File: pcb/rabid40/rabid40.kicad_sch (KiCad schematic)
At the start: 115 parts, among them J1 MX-NoLED, K1 MX-NoLED, M1 MX-NoLED, P1 MX-NoLED, Q1 MX-NoLED, SW1 SW_PUSH, T1 MX-NoLED, U1 ATmega32U4-A, U2 MX-NoLED, X1 MX-NoLED, Y1 16MHz, Y2 MX-NoLED

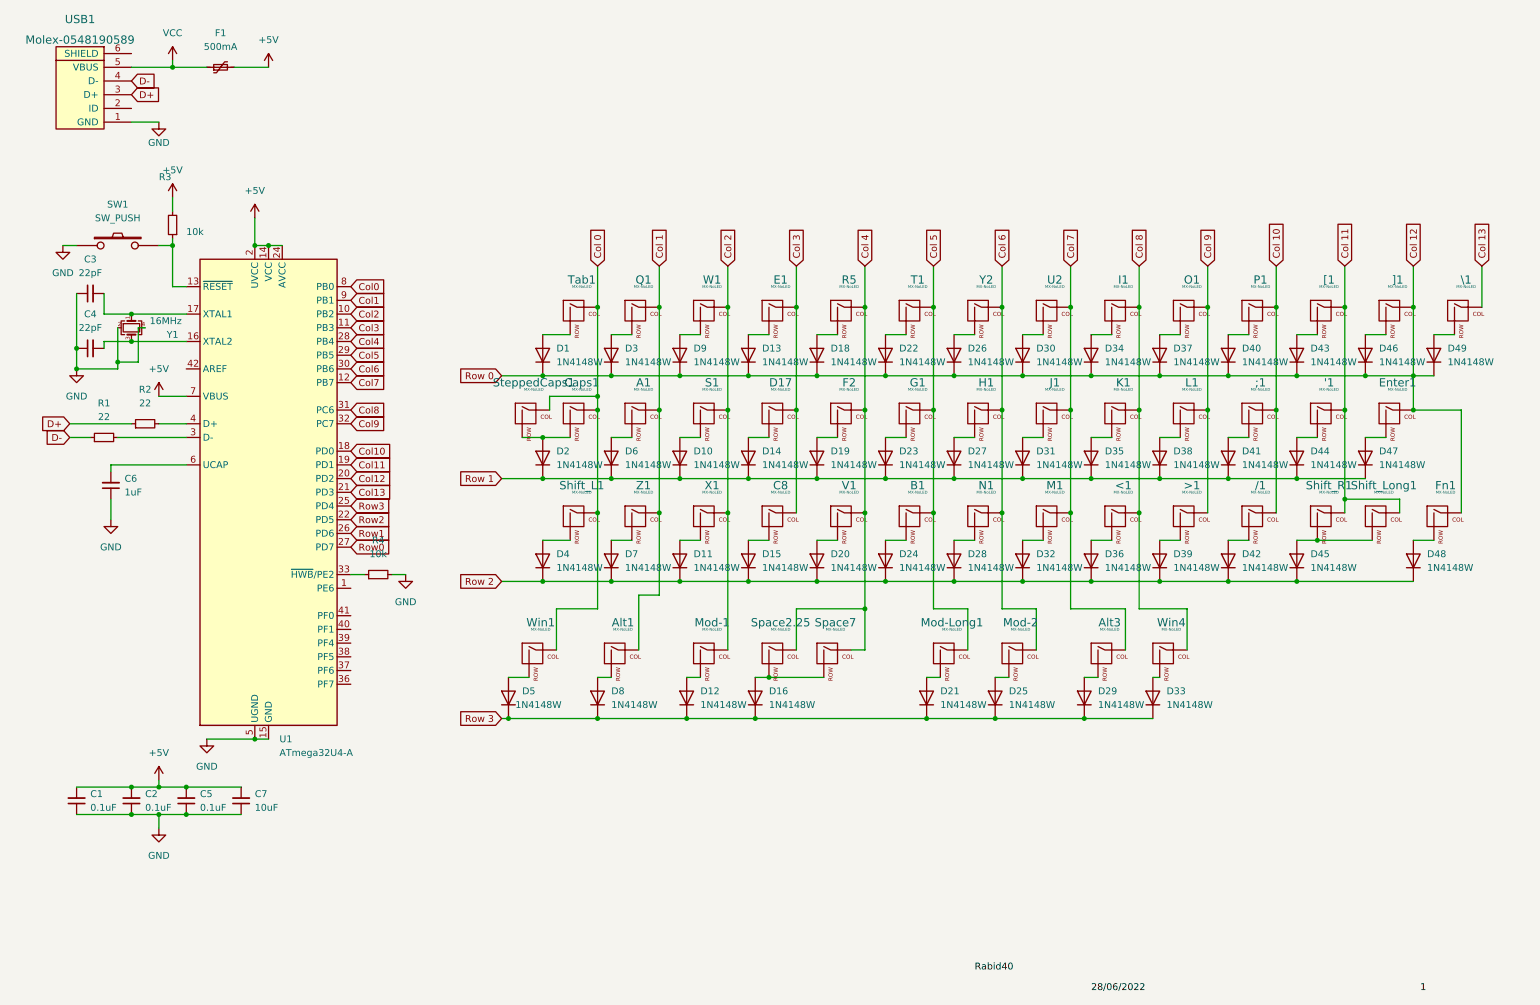
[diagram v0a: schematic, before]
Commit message: reset schematic, added submodules
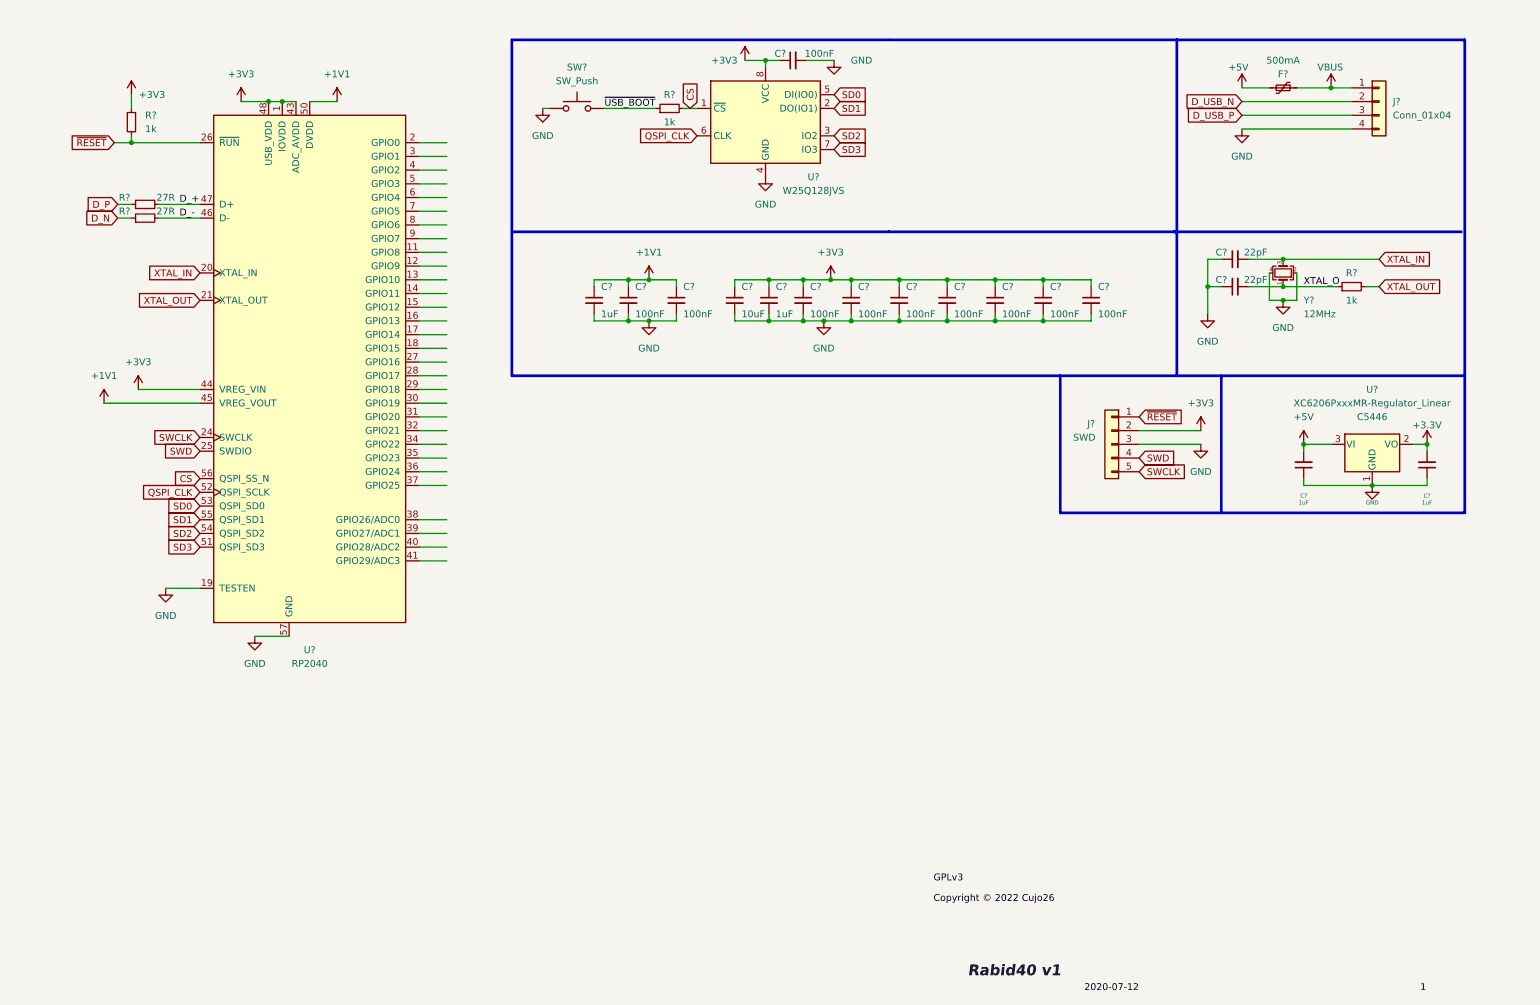
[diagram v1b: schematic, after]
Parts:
- removed '1, /1, ;1, <1, >1, A1, B1, C8, D17, E1, F2, Fn1, G1, H1, I1, J1, K1, L1, M1, Mod-1, Mod-2, N1, O1, P1, Q1, R5, S1, SteppedCaps1, T1, U2, V1, W1, Win1, Win4, X1, Y2, Z1, [1, ]1: MX-NoLED, MX_Alps_Hybrid:MX-1U, symbol ai03-mx-alps-hybrid:MX-NoLED
- removed Alt1, Alt3, Tab1, \1: MX-NoLED, MX_Alps_Hybrid:MX-1.5U, symbol ai03-mx-alps-hybrid:MX-NoLED
- removed C1, C2, C5: 0.1uF, Capacitor_SMD:C_0805_2012Metric, symbol Device:C_Small
- removed C3, C4: 22pF, Capacitor_SMD:C_0805_2012Metric, symbol Device:C_Small
- removed C6: 1uF, Capacitor_SMD:C_0805_2012Metric, symbol Device:C_Small
- removed C7: 10uF, Capacitor_SMD:C_0805_2012Metric, symbol Device:C_Small
- removed Caps1, Shift_R1: MX-NoLED, MX_Alps_Hybrid:MX-1.75U, symbol ai03-mx-alps-hybrid:MX-NoLED
- removed D1, D10, D11, D12, D13, D14, D15, D16, D18, D19, D2, D20, D21, D22, D23, D24, D25, D26, D27, D28, D29, D3, D30, D31, D32, D33, D34, D35, D36, D37, D38, D39, D4, D40, D41, D42, D43, D44, D45, D46, D47, D48, D49, D5, D6, D7, D8, D9: 1N4148W, Diode_SMD:D_SOD-123, symbol Diode:1N4148W
- removed Enter1, Shift_L1, Space2.25: MX-NoLED, MX_Alps_Hybrid:MX-2.25U, symbol ai03-mx-alps-hybrid:MX-NoLED
- removed F1: 500mA, Fuse:Fuse_1206_3216Metric, symbol Device:Polyfuse_Small
- removed Mod-Long1, Shift_Long1: MX-NoLED, MX_Alps_Hybrid:MX-2.75U, symbol ai03-mx-alps-hybrid:MX-NoLED
- removed R1, R2: 22, Resistor_SMD:R_0805_2012Metric, symbol Device:R_Small
- removed R3, R4: 10k, Resistor_SMD:R_0805_2012Metric, symbol Device:R_Small
- removed SW1: SW_PUSH, random-keyboard-parts:SKQG-1155865, symbol Keyboard_Symbols:SW_PUSH
- removed Space7: MX-NoLED, MX_Alps_Hybrid:MX-7U, symbol ai03-mx-alps-hybrid:MX-NoLED
- removed U1: ATmega32U4-A, Package_QFP:TQFP-44_10x10mm_P0.8mm, symbol MCU_Microchip_ATmega:ATmega32U4-A
- removed USB1: Molex-0548190589, random-keyboard-parts:Molex-0548190589, symbol ai03-random-parts:Molex-0548190589
- removed Y1: 16MHz, Crystal:Crystal_SMD_3225-4Pin_3.2x2.5mm, symbol Device:Crystal_GND24_Small
- added C? (x2): 22pF, Capacitor_SMD:C_0402_1005Metric, symbol Device:C_Small
- added C? (x4): 1uF, Capacitor_SMD:C_0402_1005Metric, symbol Device:C_Small
- added C? (x10): 100nF, Capacitor_SMD:C_0402_1005Metric, symbol Device:C_Small
- added C?: 10uF, Capacitor_SMD:C_0402_1005Metric, symbol Device:C_Small
- added F?: 500mA, Fuse:Fuse_1206_3216Metric, symbol Device:Polyfuse_Small
- added J?: SWD, Connector_PinSocket_2.54mm:PinSocket_1x05_P2.54mm_Vertical, symbol Connector_Generic:Conn_01x05
- added J?: Conn_01x04, symbol Connector_Generic:Conn_01x04
- added R? (x2): 27R, Resistor_SMD:R_0603_1608Metric, symbol Device:R_Small
- added R? (x3): 1k, Resistor_SMD:R_0402_1005Metric, symbol Device:R_Small
- added SW?: SW_Push, Connector_PinSocket_2.54mm:PinSocket_1x02_P2.54mm_Vertical, symbol Switch:SW_Push
- added U?: W25Q128JVS, Package_SO:SOIC-8_5.23x5.23mm_P1.27mm, symbol Memory_Flash:W25Q128JVS
- added U?: RP2040, Sleep-Lib:RP2040-QFN-56, symbol Sleep-lib:RP2040
- added U?: XC6206PxxxMR-Regulator_Linear, Package_TO_SOT_SMD:SOT-23, symbol kicad-keyboard-parts:XC6206PxxxMR-Regulator_Linear
- added Y?: 12MHz, Crystal:Crystal_SMD_3225-4Pin_3.2x2.5mm, symbol Device:Crystal_GND24_Small
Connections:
- net +5V: now also C?.2, F?.2, U?.3 (VI)
- net GND: now also C?.1, C?.1, C?.1, C?.1, C?.2, C?.2, C?.2, C?.2, C?.2, C?.2, C?.2, C?.2, C?.2, C?.2, C?.2, C?.2, C?.2, J?.3 (Pin_3), J?.4 (Pin_4), SW?.1, U?.1 (GND), U?.19 (TESTEN), U?.4 (GND), U?.57 (GND), Y?.2, Y?.4
- new net +1V1: C?.1, C?.1, C?.1, U?.23 (DVDD), U?.45 (VREG_VOUT), U?.50 (DVDD)
- new net +3V3: C?.1, C?.1, C?.1, C?.1, C?.1, C?.1, C?.1, C?.1, C?.1, C?.1, C?.2, J?.2 (Pin_2), R?.1, U?.1 (IOVDD), U?.10 (IOVDD), U?.2 (VO), U?.22 (IOVDD), U?.33 (IOVDD), U?.42 (IOVDD), U?.43 (ADC_AVDD), U?.44 (VREG_VIN), U?.48 (USB_VDD), U?.49 (IOVDD), U?.8 (VCC)
- new net CS: R?.2, U?.1 (~{CS}), U?.56 (QSPI_SS_N)
- new net D_+: R?.2, U?.47 (D+)
- new net D_-: R?.2, U?.46 (D-)
- new net D_N: R?.1
- new net D_P: R?.1
- new net D_USB_N: J?.2 (Pin_2)
- new net D_USB_P: J?.3 (Pin_3)
- new net QSPI_CLK: U?.52 (QSPI_SCLK), U?.6 (CLK)
- new net SD0: U?.5 (DI(IO0)), U?.53 (QSPI_SD0)
- new net SD1: U?.2 (DO(IO1)), U?.55 (QSPI_SD1)
- new net SD2: U?.3 (IO2), U?.54 (QSPI_SD2)
- new net SD3: U?.51 (QSPI_SD3), U?.7 (IO3)
- new net SWCLK: J?.5 (Pin_5), U?.24 (SWCLK)
- new net SWD: J?.4 (Pin_4), U?.25 (SWDIO)
- new net VBUS: F?.1, J?.1 (Pin_1)
- new net XTAL_IN: C?.2, U?.20 (XTAL_IN), Y?.3
- new net XTAL_O: C?.2, R?.1, Y?.1
- new net XTAL_OUT: R?.2, U?.21 (XTAL_OUT)
- new net ~{RESET}: J?.1 (Pin_1), R?.2, U?.26 (~{RUN})
- new net ~{USB_BOOT}: R?.1, SW?.2

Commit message: files organised
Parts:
- removed C? (x2): 1uF, Capacitor_SMD:C_0402_1005Metric, symbol Device:C_Small
- removed J?: SWD, Connector_PinSocket_2.54mm:PinSocket_1x05_P2.54mm_Vertical, symbol Connector_Generic:Conn_01x05
- removed U?: XC6206PxxxMR-Regulator_Linear, Package_TO_SOT_SMD:SOT-23, symbol kicad-keyboard-parts:XC6206PxxxMR-Regulator_Linear
- added '1, /1, ;1, <1, >1, A1, Alt1, Alt2, B1, C18, D46, E1, Enter1, F2, Fn1, G1, H1, I1, J3, K1, L1, LMod1, M1, N1, O1, P1, Q1, R6, RMod1, S1, Shift1, Shift2, Shift3, Space2.25, Space2.75, Space_7u1, T1, U4, V1, W1, Win1, Win2, X1, Y2, Z1, [1, ]1: MX_SW_solder, marbastlib-mx:SW_MX_1u, symbol marbastlib-mx:MX_SW_solder
- added Bspc1, Tab1: MX_SW_solder, marbastlib-mx:SW_MX_1.5u, symbol marbastlib-mx:MX_SW_solder
- added C11, C15: 1uF, Capacitor_SMD:C_0402_1005Metric, symbol Device:C_Small
- added Ctrl1: MX_SW_solder, marbastlib-mx:SW_MX_1.75u, symbol marbastlib-mx:MX_SW_solder
- added D1, D10, D11, D12, D13, D14, D15, D16, D17, D18, D19, D2, D20, D21, D22, D23, D24, D25, D26, D27, D28, D29, D3, D30, D31, D32, D33, D34, D35, D36, D37, D38, D39, D4, D40, D41, D42, D43, D44, D47, D48, D49, D5, D50, D52, D6, D7, D8, D9: 1N4148W, Diode_SMD:D_SOD-123, symbol Diode:1N4148W
- added J1: SWD, Connector_PinSocket_2.54mm:PinSocket_1x05_P2.54mm_Vertical, symbol Connector_Generic:Conn_01x05
- added Stab_Enter1, Stab_LShift1: MX_stab, marbastlib-mx:STAB_MX_2.25u, symbol marbastlib-mx:MX_stab
- added Stab_RShift1: MX_stab, marbastlib-mx:STAB_MX_2.75u, symbol marbastlib-mx:MX_stab
- added Stab_Spc2.25: MX_stab, marbastlib-mx:STAB_MX_P_2.25u, symbol marbastlib-mx:MX_stab
- added Stab_Spc2.75: MX_stab, marbastlib-mx:STAB_MX_P_2.75u, symbol marbastlib-mx:MX_stab
- added Stab_Spc7u1: MX_stab, marbastlib-mx:STAB_MX_P_7u, symbol marbastlib-mx:MX_stab
- added StepCtrl1: MX_SW_solder, marbastlib-mx:SW_MX_1.75u_stp, symbol marbastlib-mx:MX_SW_solder
- added U3: XC6206PxxxMR-Regulator_Linear, Package_TO_SOT_SMD:SOT-23, symbol kicad-keyboard-parts:XC6206PxxxMR-Regulator_Linear
- J2: renamed from J?; footprint (none) -> Connector_JST:JST_EH_S4B-EH_1x04_P2.50mm_Horizontal
- U1: renamed from U?; footprint Sleep-Lib:RP2040-QFN-56 -> Sleep-lib:RP2040-QFN-56
- gave numbers to parts that had none: 24
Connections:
- net +3V3: now also C15.2, J1.2 (Pin_2), U3.2 (VO)
- net +5V: now also C11.2, U3.3 (VI)
- net GND: now also C11.1, C15.1, J1.3 (Pin_3), U3.1 (GND)
- net SWCLK: now also J1.5 (Pin_5)
- net SWD: now also J1.4 (Pin_4)
- net ~{RESET}: now also J1.1 (Pin_1)
- net Col0: now reaches U1.2 (GPIO0)
- net Col0: now also Ctrl1.1, Shift1.1, StepCtrl1.1, Tab1.1
- net Col1: now reaches U1.3 (GPIO1)
- net Col1: now also A1.1, Q1.1, Z1.1
- net Col3: now reaches U1.4 (GPIO2)
- net Col3: now also Alt1.1, C18.1, D46.1, E1.1
- net Col4: now reaches U1.5 (GPIO3)
- net Col4: now also F2.1, LMod1.1, R6.1, V1.1
- new net: A1.2, D5.2 (A)
- new net: D34.2 (A), RMod1.2
- new net: '1.2, D44.2 (A)
- new net: D48.2 (A), Enter1.2
- new net: D7.2 (A), W1.2
- new net: D31.2 (A), I1.2
- new net: B1.2, D21.2 (A)
- new net: D52.2 (A), Fn1.2
- new net: D15.2 (A), R6.2
- new net: D17.2 (A), V1.2
- new net: D8.2 (A), S1.2
- new net: D49.2 (A), Shift2.2, Shift3.2
- new net: D12.2 (A), D46.2
- new net: D39.2 (A), P1.2
- new net: D27.2 (A), U4.2
- new net: Ctrl1.2, D2.2 (A), StepCtrl1.2
- new net: D22.2 (A), Space2.25.2
- new net: D42.2 (A), Win2.2
- new net: D4.2 (A), Q1.2
- new net: >1.2, D37.2 (A)
- new net: D29.2 (A), M1.2
- new net: D6.2 (A), Z1.2
- new net: Alt1.2, D14.2 (A)
- new net: D47.2 (A), ]1.2
- new net: <1.2, D33.2 (A)
- new net: D1.2 (A), Tab1.2
- new net: D19.2 (A), T1.2
- new net: D36.2 (A), L1.2
- new net: D11.2 (A), E1.2
- new net: D10.2 (A), Win1.2
- new net: D28.2 (A), J3.2
- new net: D23.2 (A), Y2.2
- new net: Bspc1.2, D50.2 (A)
- new net: D16.2 (A), F2.2
- new net: D26.2 (A), Space_7u1.2
- new net: D35.2 (A), O1.2
- new net: Alt2.2, D38.2 (A)
- new net: /1.2, D41.2 (A)
- new net: D30.2 (A), Space2.75.2
- new net: D25.2 (A), N1.2
- new net: D3.2 (A), Shift1.2
- new net: D32.2 (A), K1.2
- new net: D43.2 (A), [1.2
- new net: D18.2 (A), LMod1.2
- new net: ;1.2, D40.2 (A)
- new net: D9.2 (A), X1.2
- new net: D20.2 (A), G1.2
- new net: C18.2, D13.2 (A)
- new net: D24.2 (A), H1.2
- new net Col10: /1.1, ;1.1, P1.1, Win2.1
- new net Col11: '1.1, [1.1
- new net Col12: Enter1.1, Shift2.1, Shift3.1, ]1.1
- new net Col13: Bspc1.1, Fn1.1
- new net Col2: S1.1, W1.1, Win1.1, X1.1
- new net Col5: B1.1, G1.1, Space2.25.1, T1.1
- new net Col6: H1.1, N1.1, Space_7u1.1, Y2.1
- new net Col7: J3.1, M1.1, Space2.75.1, U4.1
- new net Col8: <1.1, I1.1, K1.1, RMod1.1
- new net Col9: >1.1, Alt2.1, L1.1, O1.1
- new net Row0: D1.1 (K), D11.1 (K), D15.1 (K), D19.1 (K), D23.1 (K), D27.1 (K), D31.1 (K), D35.1 (K), D39.1 (K), D4.1 (K), D43.1 (K), D47.1 (K), D50.1 (K), D7.1 (K)
- new net Row1: D12.1 (K), D16.1 (K), D2.1 (K), D20.1 (K), D24.1 (K), D28.1 (K), D32.1 (K), D36.1 (K), D40.1 (K), D44.1 (K), D48.1 (K), D5.1 (K), D8.1 (K)
- new net Row2: D13.1 (K), D17.1 (K), D21.1 (K), D25.1 (K), D29.1 (K), D3.1 (K), D33.1 (K), D37.1 (K), D41.1 (K), D49.1 (K), D52.1 (K), D6.1 (K), D9.1 (K)
- new net Row3: D10.1 (K), D14.1 (K), D18.1 (K), D22.1 (K), D26.1 (K), D30.1 (K), D34.1 (K), D38.1 (K), D42.1 (K)
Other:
- moved on the sheet: C1, C10, C12, C13, C14, C16, C17, C2, C3, C4, C5, C6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

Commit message: moved some mcu components into place
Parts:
- C1, C5: Note (none) -> Close to pin 44 and 45
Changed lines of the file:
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@@
+      (effects (font (size 1.27 1.27)) hide)
+    )
+    (property "Note" "Close to pin 44 and 45" (id 5) (at 148.59 63.5 0)
       (effects (font (size 1.27 1.27)) hide)
     )
@@
       (effects (font (size 1.27 1.27)) hide)
     )
+    (property "Note" "Close to pin 44 and 45" (id 5) (at 116.205 63.5 0)
+      (effects (font (size 1.27 1.27)) hide)
+    )

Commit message: completed routing
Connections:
- net D_USB_N is gone; now on net D_N: J2.2 (Pin_2)
- net D_USB_P is gone; now on net D_P: J2.3 (Pin_3)
- net Col0: now also U1.27 (GPIO16); no longer U1.2 (GPIO0)
- net Col1: now also U1.28 (GPIO17); no longer U1.3 (GPIO1)
- net Col10: now also U1.7 (GPIO5)
- net Col11: now also U1.8 (GPIO6)
- net Col12: now also U1.9 (GPIO7)
- net Col13: now also U1.11 (GPIO8)
- net Col2: now also U1.29 (GPIO18)
- net Col3: now also U1.36 (GPIO24); no longer U1.4 (GPIO2)
- net Col4: now also U1.35 (GPIO23); no longer U1.5 (GPIO3)
- net Col5: now also U1.2 (GPIO0)
- net Col6: now also U1.3 (GPIO1)
- net Col7: now also U1.4 (GPIO2)
- net Col8: now also U1.5 (GPIO3)
- net Col9: now also U1.6 (GPIO4)
- net Row0: now also U1.41 (GPIO29/ADC3)
- net Row1: now also U1.30 (GPIO19)
- net Row2: now also U1.39 (GPIO27/ADC1)
- net Row3: now also U1.38 (GPIO26/ADC0)

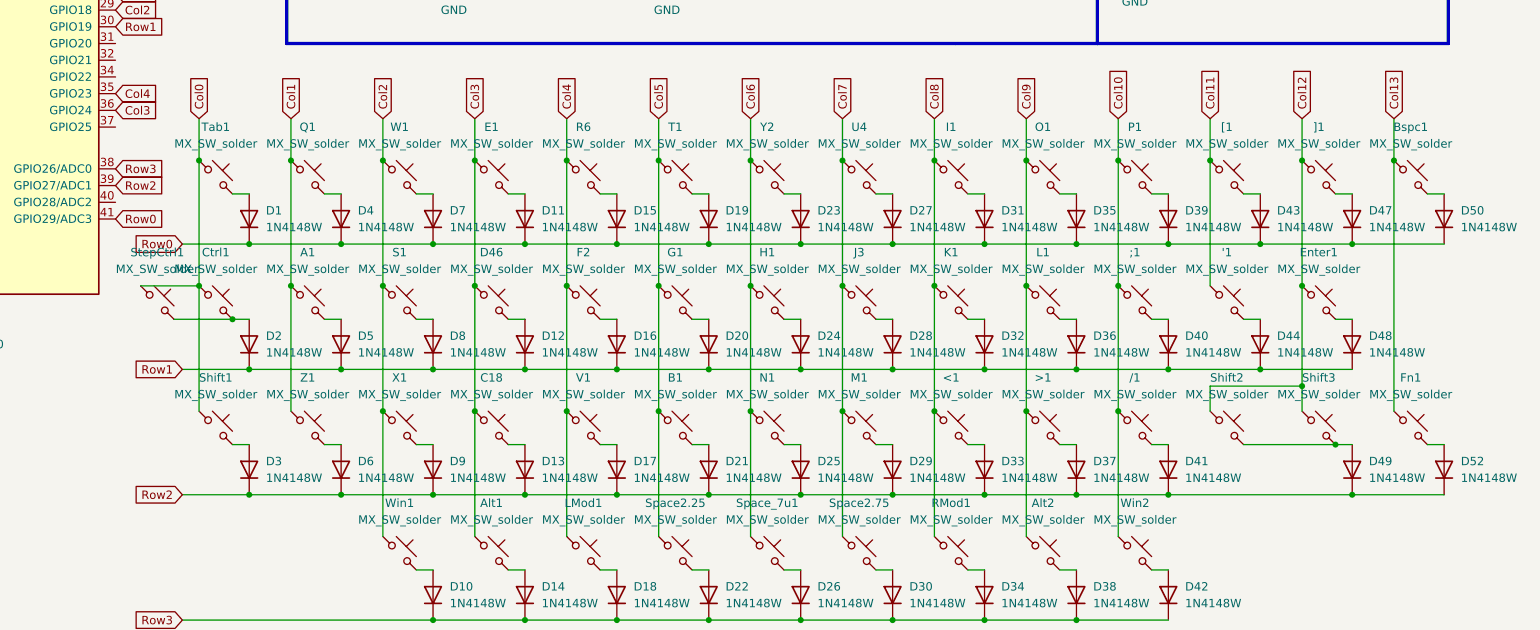
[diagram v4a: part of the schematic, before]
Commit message: fixed some issues to make it manufacturable at jlcpcb
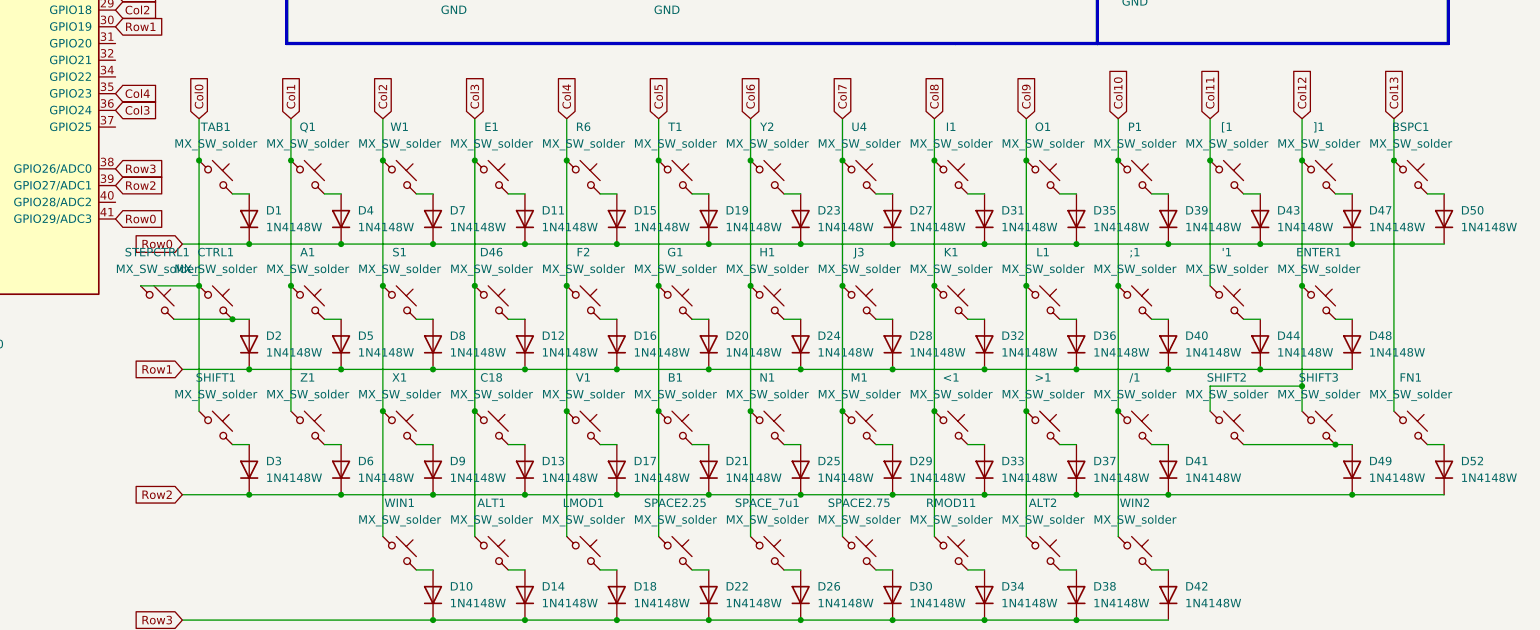
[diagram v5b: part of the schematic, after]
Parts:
- J2: footprint Connector_JST:JST_EH_S4B-EH_1x04_P2.50mm_Horizontal -> Connector_JST:JST_SH_SM04B-SRSS-TB_1x04-1MP_P1.00mm_Horizontal
- renumbered Alt1 to ALT1, Alt2 to ALT2, Bspc1 to BSPC1, Ctrl1 to CTRL1, Enter1 to ENTER1, Fn1 to FN1, LMod1 to LMOD1, RMod1 to RMOD11, Shift1 to SHIFT1, Shift2 to SHIFT2, Shift3 to SHIFT3, Space2.25 to SPACE2.25, Space2.75 to SPACE2.75, Space_7u1 to SPACE_7u1, StepCtrl1 to STEPCTRL1, Tab1 to TAB1, Win1 to WIN1, Win2 to WIN2
